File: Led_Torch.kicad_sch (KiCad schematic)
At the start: 4 parts, among them SW1 SW_DPST_x2

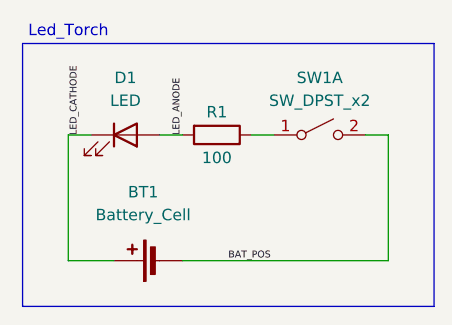
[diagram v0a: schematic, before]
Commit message: Update: revised schematic/PCB layout, regenerated Gerbers/STEP/views, added copper fill 2D views, fixed company name
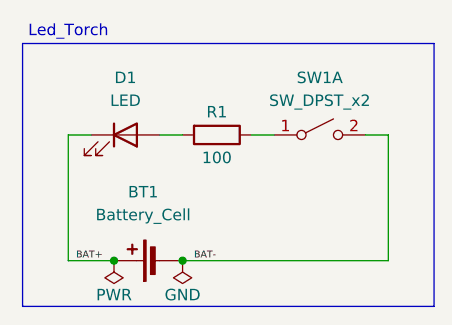
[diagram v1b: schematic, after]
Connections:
- net BAT_POS renamed BAT-
- net LED_ANODE: no longer names the net of D1.2 (A), R1.2
- net LED_CATHODE renamed BAT+
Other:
- company: IBrahim Jarallah -> Ibrahim Jarallah
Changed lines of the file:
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@@
 		(date "2026-03-01")
 		(rev "1.0")
-		(company "IBrahim Jarallah")
+		(company "Ibrahim Jarallah")
 	)
 	(text "Led_Torch"
@@
 		)
 	)
+	(junction
+		(at 132.08 92.71)
+		(diameter 0)
+		(color 0 0 0 0)
+	)
+	(junction
+		(at 124.46 92.71)
+		(diameter 0)
+		(color 0 0 0 0)
+	)
 	(wire
 		(pts
@@
 		)
 	)
-	(label "LED_ANODE"
-		(at 132.08 78.74 90)
+	(label "BAT-"
+		(at 133.35 92.71 0)
 		(effects
 			(font
@@
 		)
 	)
-	(label "BAT_POS"
-		(at 137.16 92.71 0)
+	(label "BAT+"
+		(at 123.19 92.71 180)
 		(effects
 			(font
 				(size 0.762 0.762)
 			)
-			(justify left bottom)
-		)
-	)
-	(label "LED_CATHODE"
-		(at 120.65 78.74 90)
-		(effects
-			(font
-				(size 0.762 0.762)
-			)
-			(justify left bottom)
+			(justify right bottom)
 		)
 	)
@@
 					(unit 1)
 				)
+			)
+		)
+	)
+	(symbol
+		(lib_id "power:PWR_FLAG")
+		(at 124.46 92.71 180)
+		(unit 1)
+		(exclude_from_sim no)
+		(in_bom yes)
+		(on_board yes)
+		(dnp no)
+		(property "Reference" "#FLG01"
+			(at 124.46 94.615 0)
+			(effects
+				(font
+					(size 1.27 1.27)
+				)
+				(hide yes)
+			)
+		)
+		(property "Value" "PWR"
+			(at 124.46 96.52 0)
+			(effects
+				(font
+					(size 1.27 1.27)
+				)
+			)
+		)
+		(property "Footprint" ""
+			(at 124.46 92.71 0)
+			(effects
+				(font
+					(size 1.27 1.27)
+				)
+				(hide yes)
+			)
+		)
+		(property "Datasheet" "~"
+			(at 124.46 92.71 0)
+			(effects
+				(font
+					(size 1.27 1.27)
+				)
+				(hide yes)
+			)
+		)
+		(property "Description" "Special symbol for telling ERC where power comes from"
+			(at 124.46 92.71 0)
+			(effects
+				(font
+					(size 1.27 1.27)
+				)
+				(hide yes)
+			)
+		)
+		(pin "1"
+		)
+		(instances
+			(project ""
+				(path "/8fde1427-f0f9-4abc-b6a5-00700d695800"
+					(reference "#FLG01")
+					(unit 1)
+				)
+			)
+		)
+	)
+	(symbol
+		(lib_id "power:PWR_FLAG")
+		(at 132.08 92.71 180)
+		(unit 1)
+		(exclude_from_sim no)
+		(in_bom yes)
+		(on_board yes)
+		(dnp no)
+		(property "Reference" "#FLG02"
+			(at 132.08 94.615 0)
+			(effects
+				(font
+					(size 1.27 1.27)
+				)
+				(hide yes)
+			)
+		)
+		(property "Value" "GND"
+			(at 132.08 96.52 0)
+			(effects
+				(font
+					(size 1.27 1.27)
+				)
+			)
+		)
+		(property "Footprint" ""
+			(at 132.08 92.71 0)
+			(effects
+				(font
+					(size 1.27 1.27)
+				)
+				(hide yes)
+			)
+		)
+		(property "Datasheet" "~"
+			(at 132.08 92.71 0)
+			(effects
+				(font
+					(size 1.27 1.27)
+				)
+				(hide yes)
+			)
+		)
+		(property "Description" "Special symbol for telling ERC where power comes from"
+			(at 132.08 92.71 0)
+			(effects
+				(font
+					(size 1.27 1.27)
+				)
+				(hide yes)
+			)
+		)
+		(pin "1"
+		)
+		(instances
+			(project "Led_Torch"
+				(path "/8fde1427-f0f9-4abc-b6a5-00700d695800"
+					(reference "#FLG02")
+					(unit 1)
+				)
